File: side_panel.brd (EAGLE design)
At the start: 112 x 81.7 mm, 35 parts

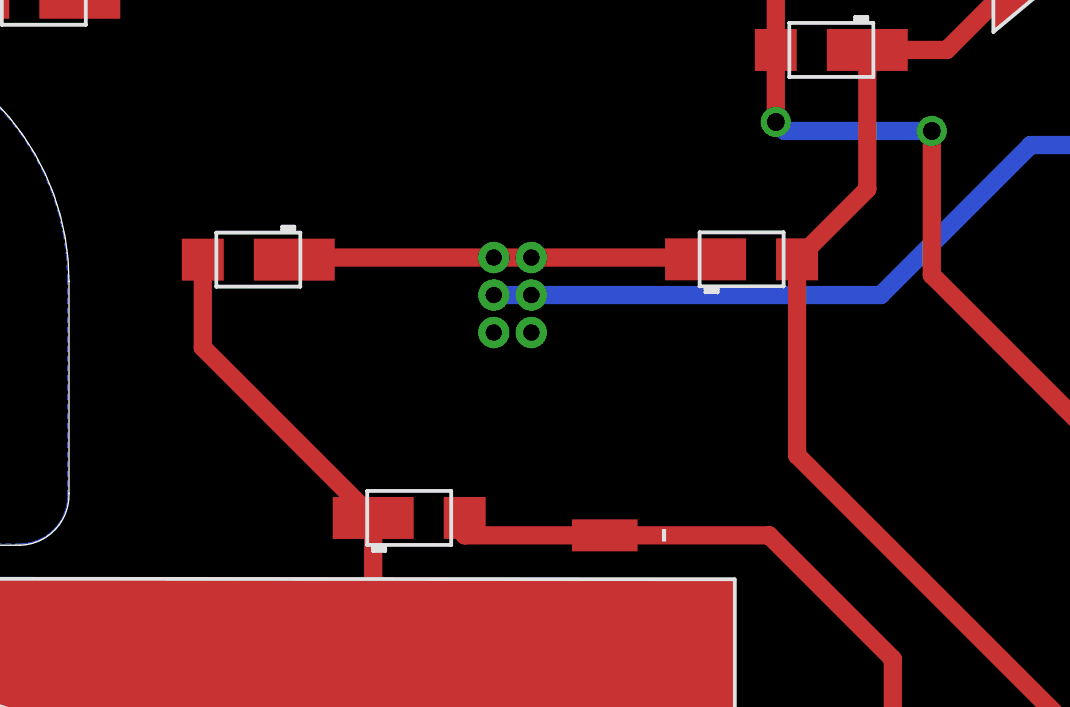
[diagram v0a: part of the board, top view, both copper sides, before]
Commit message: Updated side panel connectors
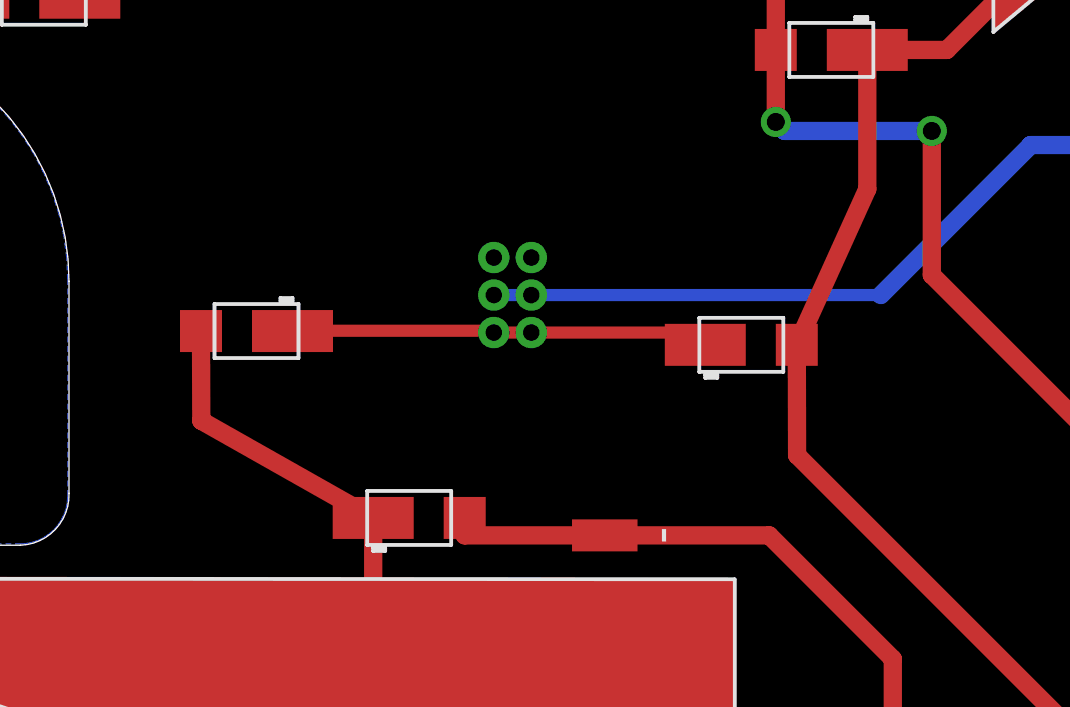
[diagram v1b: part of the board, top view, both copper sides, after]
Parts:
- moved D1 2.85 mm to (83.5, 38.8)
- moved D7 2.38 mm to (67.3, 39.2)
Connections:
- net GND: no longer U$1.P3, U$1.P6
- net V_SOLAR: now also U$1.P3, U$1.P6; no longer U$1.P1, U$1.P4
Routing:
- net N$8: track 60.7 -> 59.3 mm
- net V_SOLAR: track 13.8 -> 14.5 mm
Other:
- board text added: "Side Solar Panel V1.2"
- board text removed: "Side Solar Panel V1.1"
